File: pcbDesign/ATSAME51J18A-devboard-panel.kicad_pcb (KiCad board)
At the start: 2 copper layers, 100 x 100 mm, 294 parts, among them IC1 MP9361DJ-LF-P, J1 Micro_SD_Card, J10 CAN, J11 Conn_01x32_Male, J2 USB C, J3 QWIIC, J4 S2B-PH-K-S(LF)(SN), J7 Conn_01x32_Male, SW1 RST, U1 TCAN1051GVDRQ1, U2 ATSAME51J18A-A, U3 MIC5219-5.0YMM, U4 LM27762, U5 TPS60501DGS, U7 BQ24074RGT, U8 BQ27441DRZR-G1B, Y1 32.768

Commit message: Panelized with logo
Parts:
- removed the U2 at (93.4, 95.2)
- removed the U2 at (93.4, 63.7)
- removed the U4 at (103.5, 98.1)
- removed the U4 at (103.5, 66.6)
- added C21: 1u, Capacitor_SMD:C_0402_1005Metric, B.Cu at (107.2, 121.0)
- added C21: 1u, Capacitor_SMD:C_0402_1005Metric, B.Cu at (107.2, 89.6)
- added R12: 1.18k, Resistor_SMD:R_0402_1005Metric, B.Cu at (65.1, 130.5)
- added R12: 1.18k, Resistor_SMD:R_0402_1005Metric, B.Cu at (65.1, 99.1)
- U2 (x2): renamed from R12; value 1.18k -> ATSAME51J18A-A; footprint Resistor_SMD:R_0402_1005Metric -> Package_QFP:TQFP-64_10x10mm_P0.5mm; moved to F.Cu
- U4 (x2): renamed from C21; value 1u -> LM27762; footprint Capacitor_SMD:C_0402_1005Metric -> Package_SON:WSON-12-1EP_3x2mm_P0.5mm_EP1x2.65_ThermalVias
- moved U2 45.3 mm to (93.4, 95.2)
- moved U2 45.3 mm to (93.4, 63.7)
- moved U4 23.2 mm to (103.5, 98.1), turned to 0 degrees
- moved U4 23.2 mm to (103.5, 66.6), turned to 0 degrees
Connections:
- U2 pad 1: Board_3-GND -> Board_2-Net-(C4-Pad2)
- U2 pad 2: Board_3-Net-(R12-Pad2) -> Board_2-Net-(C3-Pad1)
- U2 pad 1: Board_2-GND -> Board_1-Net-(C4-Pad2)
- U2 pad 2: Board_2-Net-(R12-Pad2) -> Board_1-Net-(C3-Pad1)
- U4 pad 1: Board_3-Net-(C21-Pad1) -> Board_2-Net-(R6-Pad1)
- U4 pad 2: Board_3-Net-(C21-Pad2) -> Board_2-Net-(C15-Pad1)
- U4 pad 1: Board_2-Net-(C21-Pad1) -> Board_1-Net-(R6-Pad1)
- U4 pad 2: Board_2-Net-(C21-Pad2) -> Board_1-Net-(C15-Pad1)

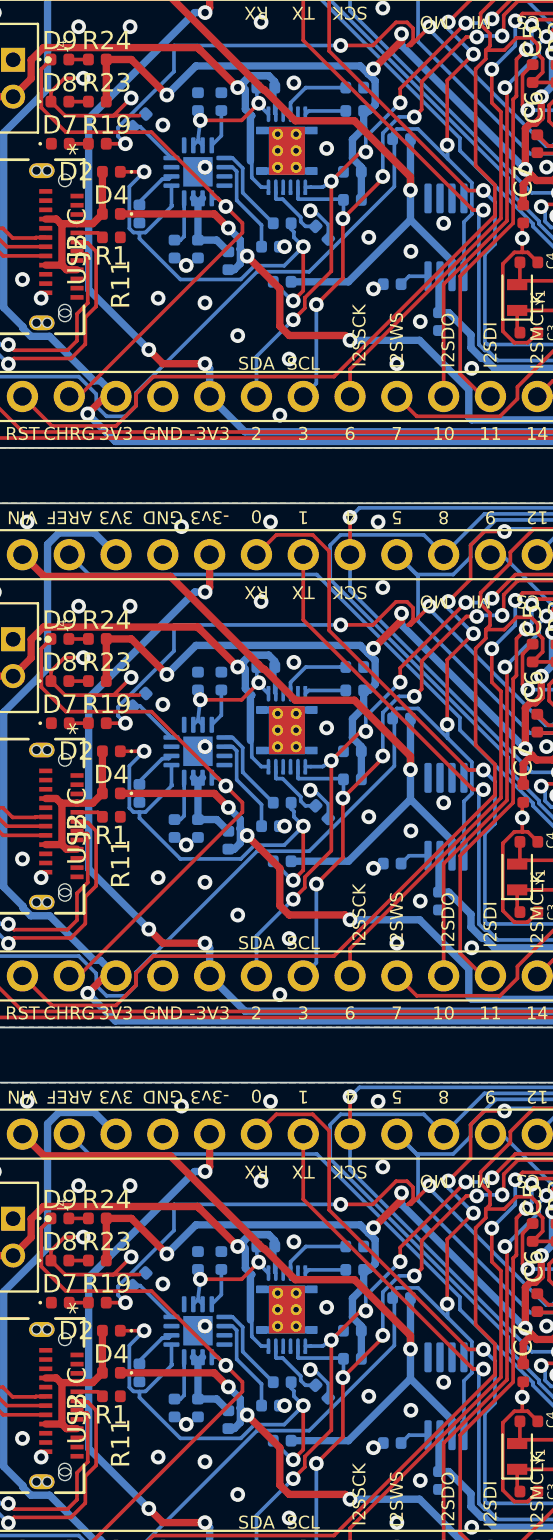
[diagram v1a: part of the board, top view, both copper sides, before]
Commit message: Panelized with logo
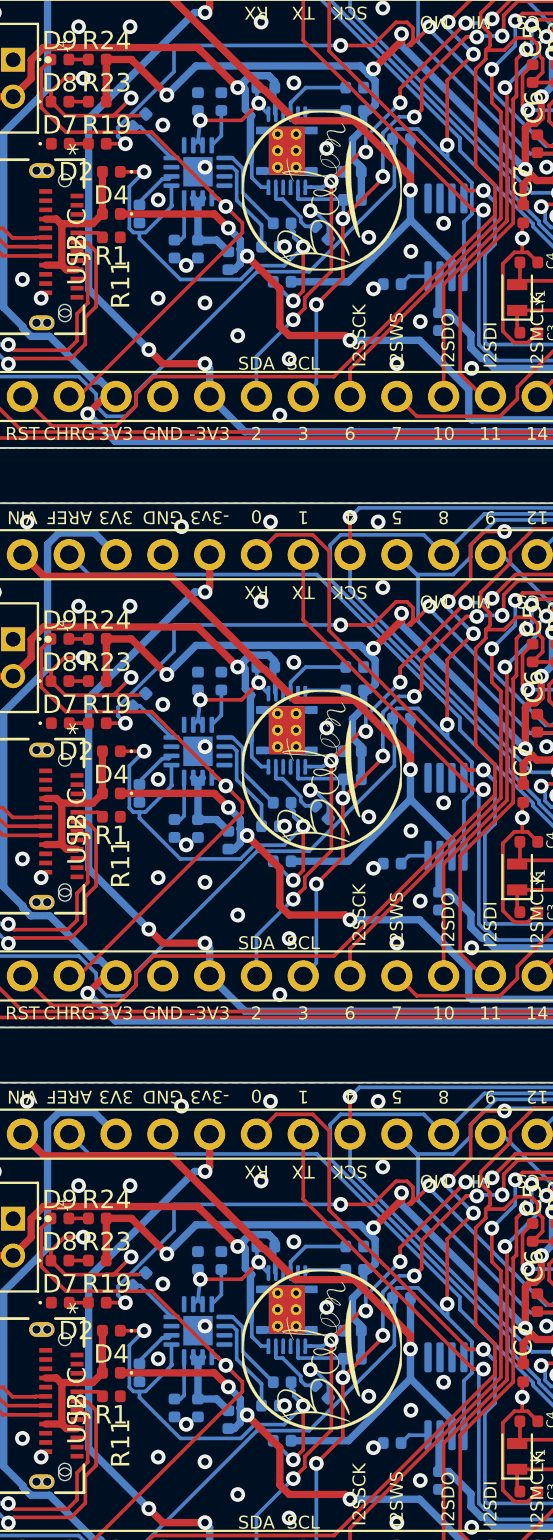
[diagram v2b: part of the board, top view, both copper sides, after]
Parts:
- removed the C18 at (112.7, 128.6)
- removed the C19 at (107.4, 123.8)
- removed the C20 at (102.3, 119.0)
- removed the C21 at (107.2, 121.0)
- removed the C22 at (66.4, 130.5)
- removed the C24 at (73.1, 129.7)
- removed the D4 at (61.7, 97.2)
- removed the R13 at (63.2, 123.6)
- removed the R14 at (74.8, 126.4)
- removed the R15 at (74.8, 127.9)
- removed the R16 at (70.1, 121.8)
- removed the R17 at (74.9, 121.8)
- removed the R18 at (74.9, 123.1)
- removed the R19 at (60.9, 124.8)
- added C1: 100n, Capacitor_SMD:C_0402_1005Metric, B.Cu at (123.2, 133.5)
- added C2: 100n, Capacitor_SMD:C_0402_1005Metric, B.Cu at (121.9, 123.3)
- added C3: 22u, Capacitor_SMD:C_0402_1005Metric, F.Cu at (84.3, 135.1)
- added C4: 22u, Capacitor_SMD:C_0402_1005Metric, F.Cu at (84.3, 131.3)
- added C5: 1u, Capacitor_SMD:C_0402_1005Metric, F.Cu at (84.5, 121.0)
- added C6: 1u, Capacitor_SMD:C_0402_1005Metric, F.Cu at (84.8, 124.8)
- added C7: 500n, Capacitor_SMD:C_0402_1005Metric, F.Cu at (84.0, 128.6)
- added G***: LOGO, Symbol:BatonLogo, F.Cu at (73.1, 127.4)
- added G***: LOGO, Symbol:BatonLogo, F.Cu at (73.1, 95.9)
- added G***: LOGO, Symbol:BatonLogo, F.Cu at (73.1, 64.5)
- added J1: Micro_SD_Card, Connector_Card:microSD_HC_Hirose_DM3D-SF, F.Cu at (125.4, 127.1)
- added R1: 5.1k, Resistor_SMD:R_0402_1005Metric, F.Cu at (61.7, 129.9)
- added R2: 5.1k, Resistor_SMD:R_0402_1005Metric, B.Cu at (54.1, 130.4)
- added R3: 10K, Resistor_SMD:R_0402_1005Metric, F.Cu at (85.8, 121.0)
- added R4: 10k, Resistor_SMD:R_0402_1005Metric, B.Cu at (77.4, 124.6)
- added R6: 10k, Resistor_SMD:R_0402_1005Metric, B.Cu at (101.6, 132.7)
- added R7: 87.5k, Resistor_SMD:R_0402_1005Metric, B.Cu at (106.8, 131.4)
- C10: renamed from C3; value 22u -> 2.2u; moved to B.Cu
- C11: renamed from C4; value 22u -> 4.7u; moved to B.Cu
- C12: renamed from C5; value 1u -> 2.2u; moved to B.Cu
- C13: renamed from C6; value 1u -> 4.7u; moved to B.Cu
- C14: renamed from C7; value 500n -> 0.47u; moved to B.Cu
- C15: renamed from C8; value 0.47u -> 2.2u
- C16: renamed from C9; value 0.47u -> 2.2u
- C17: renamed from C10; value 2.2u -> 1u
- C18: renamed from C11; value 4.7u -> 10u
- C19: renamed from C12; value 2.2u -> 4.7u
- C20: renamed from C13; value 4.7u -> 22u
- C21: renamed from C14; value 0.47u -> 1u
- C22: renamed from C15; value 2.2u -> 4.7u
- C23: renamed from C16; value 2.2u -> 4.7u
- C24: renamed from C17; value 1u -> 0.47u
- C8: renamed from C1; value 100n -> 0.47u
- C9: renamed from C2; value 100n -> 0.47u
- D4: renamed from C23; value 4.7u -> D_Schottky; footprint Capacitor_SMD:C_0402_1005Metric -> Diode_SMD:D_0402_1005Metric; moved to F.Cu
- R10: renamed from R2; value 5.1k -> 50k
- R11: renamed from R3; value 10K -> 46.4k; moved to B.Cu
- R12: renamed from R4; value 10k -> 1.18k
- R13: renamed from R6; value 10k -> 1.13k
- R14: renamed from R7; value 87.5k -> 5.1k
- R15: renamed from R8; value 87.5k -> 5.1k
- R16: renamed from R9; value 50k -> 0.01
- R17: renamed from R10; value 50k -> 10k
- R18: renamed from R11; value 46.4k -> 10k
- R19: renamed from R12; value 1.18k -> 10k; moved to F.Cu
- R8: renamed from J1; value Micro_SD_Card -> 87.5k; footprint Connector_Card:microSD_HC_Hirose_DM3D-SF -> Resistor_SMD:R_0402_1005Metric; moved to B.Cu
- R9: renamed from R1; value 5.1k -> 50k; moved to B.Cu
- moved R10 52.7 mm to (106.6, 127.6)
- moved C8 46.2 mm to (76.9, 132.5), turned to 180 degrees
- moved R9 45.2 mm to (106.8, 133.3), turned to 270 degrees
- moved C22 41.5 mm to (66.4, 130.5), turned to 270 degrees
- moved R13 39.4 mm to (63.2, 123.6), turned to 45 degrees
- moved R16 38.5 mm to (70.1, 121.8), turned to 0 degrees
- moved C23 37.8 mm to (66.4, 122.5), turned to 90 degrees
- moved R14 32.4 mm to (74.8, 126.4), turned to 180 degrees
- moved R17 32.3 mm to (74.9, 121.8), turned to 0 degrees
- moved C23 31.4 mm to (66.4, 91.1)
- moved C10 31.4 mm to (113.0, 122.3), turned to 270 degrees
- moved C15 31.0 mm to (107.9, 131.4), turned to 90 degrees
- moved C19 29.9 mm to (107.4, 123.8)
- moved R15 29.4 mm to (74.8, 127.9), turned to 0 degrees
- moved C24 27.7 mm to (73.1, 129.7), turned to 315 degrees
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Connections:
- C10 pad 1: Board_3-Net-(C3-Pad1) -> Board_3-VBUS_NREG
- C11 pad 2: Board_3-Net-(C4-Pad2) -> Board_3-VBUS_NREG
- C12 pad 1: Board_3-GND -> Board_3-VBUS_VIN_5V_REG
- C12 pad 2: Board_3-RST -> Board_3-GND
- C13 pad 1: Board_3-GND -> Board_3-Net-(C13-Pad1)
- C13 pad 2: Board_3-Net-(C6-Pad2) -> Board_3-GND
- C14 pad 1: Board_3-GND -> Board_3-Net-(C14-Pad1)
- C14 pad 2: Board_3-VBUS_3V3_CH0_REG -> Board_3-Net-(C14-Pad2)
- C15 pad 1: Board_3-Net-(C8-Pad1) -> Board_3-Net-(C15-Pad1)
- C15 pad 2: Board_3-GND -> Board_3-VBUS_3V3_CH1_REG
- C16 pad 1: Board_3-Net-(C9-Pad1) -> Board_3-VBUS_-3V3_CH2_REG
- C16 pad 2: Board_3-Net-(C9-Pad2) -> Board_3-Net-(C16-Pad2)
- C17 pad 1: Board_3-VBUS_NREG -> Board_3-Net-(C17-Pad1)
- C17 pad 2: Board_3-GND -> Board_3-Net-(C17-Pad2)
- C18 pad 2: Board_3-VBUS_NREG -> Board_3-+5V
- C19 pad 1: Board_3-VBUS_VIN_5V_REG -> Board_3-VBUS_NREG
- C20 pad 1: Board_3-Net-(C13-Pad1) -> Board_3-GND
- C20 pad 2: Board_3-GND -> Board_3-VBUS_3V3_CH0_REG
- C21 pad 1: Board_3-Net-(C14-Pad1) -> Board_3-Net-(C21-Pad1)
- C21 pad 2: Board_3-Net-(C14-Pad2) -> Board_3-Net-(C21-Pad2)
- C22 pad 1: Board_3-Net-(C15-Pad1) -> Board_3-VBUS_BAT_NREG
- C22 pad 2: Board_3-VBUS_3V3_CH1_REG -> Board_3-GND
- C23 pad 1: Board_3-VBUS_-3V3_CH2_REG -> Board_3-Net-(C23-Pad1)
- C23 pad 2: Board_3-Net-(C16-Pad2) -> Board_3-GND
- C23 pad 1: Board_3-Net-(C23-Pad1) -> Board_2-Net-(C23-Pad1)
- C23 pad 2: Board_3-GND -> Board_2-GND
- C24 pad 1: Board_3-Net-(C17-Pad1) -> Board_3-Net-(C24-Pad1)
- C24 pad 2: Board_3-Net-(C17-Pad2) -> Board_3-GND
- C8 pad 1: Board_3-GND -> Board_3-Net-(C8-Pad1)
- C8 pad 2: Board_3-VBUS_3V3_CH0_REG -> Board_3-GND
- C9 pad 1: Board_3-GND -> Board_3-Net-(C9-Pad1)
- C9 pad 2: Board_3-+5V -> Board_3-Net-(C9-Pad2)
- D4 pad 1: Board_2-Net-(C23-Pad1) -> Board_2-VBUS_NREG
- D4 pad 2: Board_2-GND -> Board_2-VBUS_USB_NREG
- R10 pad 1: Board_3-Net-(J2-PadB5) -> Board_3-GND
- R10 pad 2: Board_3-GND -> Board_3-Net-(C16-Pad2)
- R11 pad 1: Board_3-RST -> Board_3-GND
- R11 pad 2: Board_3-VBUS_3V3_CH0_REG -> Board_3-Net-(R11-Pad2)
- R12 pad 1: Board_3-VBUS_VIN_NREG -> Board_3-GND
- R12 pad 2: Board_3-EN -> Board_3-Net-(R12-Pad2)
- R13 pad 1: Board_3-Net-(R6-Pad1) -> Board_3-Net-(R13-Pad1)
- R13 pad 2: Board_3-VBUS_NREG -> Board_3-GND
- R14 pad 1: Board_3-VBUS_3V3_CH1_REG -> Board_3-VBUS_3V3_CH0_REG
- R14 pad 2: Board_3-Net-(C15-Pad1) -> Board_3-2[SDA]
- R15 pad 1: Board_3-Net-(C16-Pad2) -> Board_3-3[SCL]
- R15 pad 2: Board_3-VBUS_-3V3_CH2_REG -> Board_3-VBUS_3V3_CH0_REG
- R16 pad 1: Board_3-Net-(C15-Pad1) -> Board_3-Net-(C23-Pad1)
- R16 pad 2: Board_3-GND -> Board_3-VBUS_BAT
- R17 pad 1: Board_3-GND -> Board_3-Net-(R17-Pad1)
- R17 pad 2: Board_3-Net-(C16-Pad2) -> Board_3-GND
- R18 pad 1: Board_3-GND -> Board_3-Net-(R18-Pad1)
- R18 pad 2: Board_3-Net-(R11-Pad2) -> Board_3-VBUS_3V3_CH0_REG
- R19 pad 1: Board_3-GND -> Board_3-13
- R19 pad 2: Board_3-Net-(R12-Pad2) -> Board_3-Net-(D7-Pad2)
- R8 pad 1: (no net) -> Board_3-Net-(C16-Pad2)
- R8 pad 2: Board_3-SDDAT3 -> Board_3-VBUS_-3V3_CH2_REG
- R9 pad 1: Board_3-GND -> Board_3-Net-(C15-Pad1)
- R9 pad 2: Board_3-Net-(J2-PadA5) -> Board_3-GND
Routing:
- net Board_3-GND: vias 80 -> 81
- net Board_2-GND: vias 80 -> 81
- net Board_1-GND: vias 80 -> 81

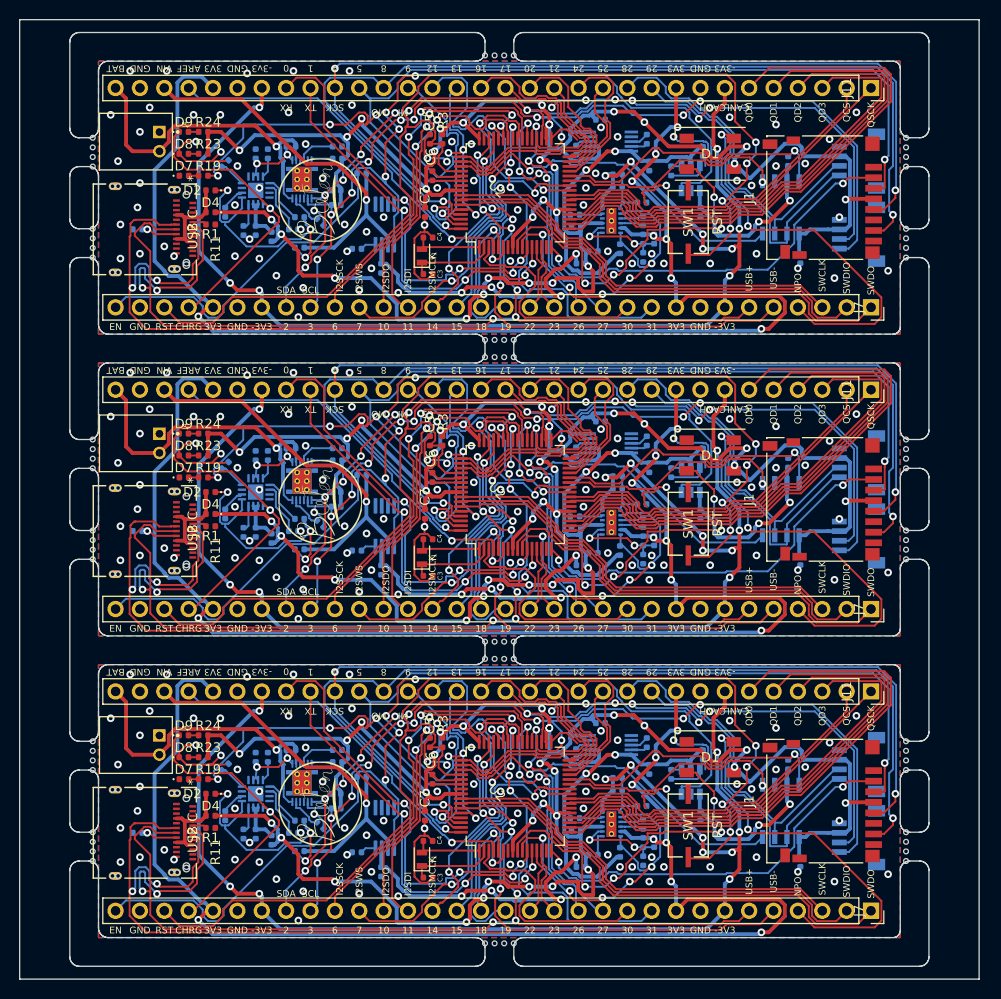
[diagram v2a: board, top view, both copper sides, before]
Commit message: Fixed some DRC errors
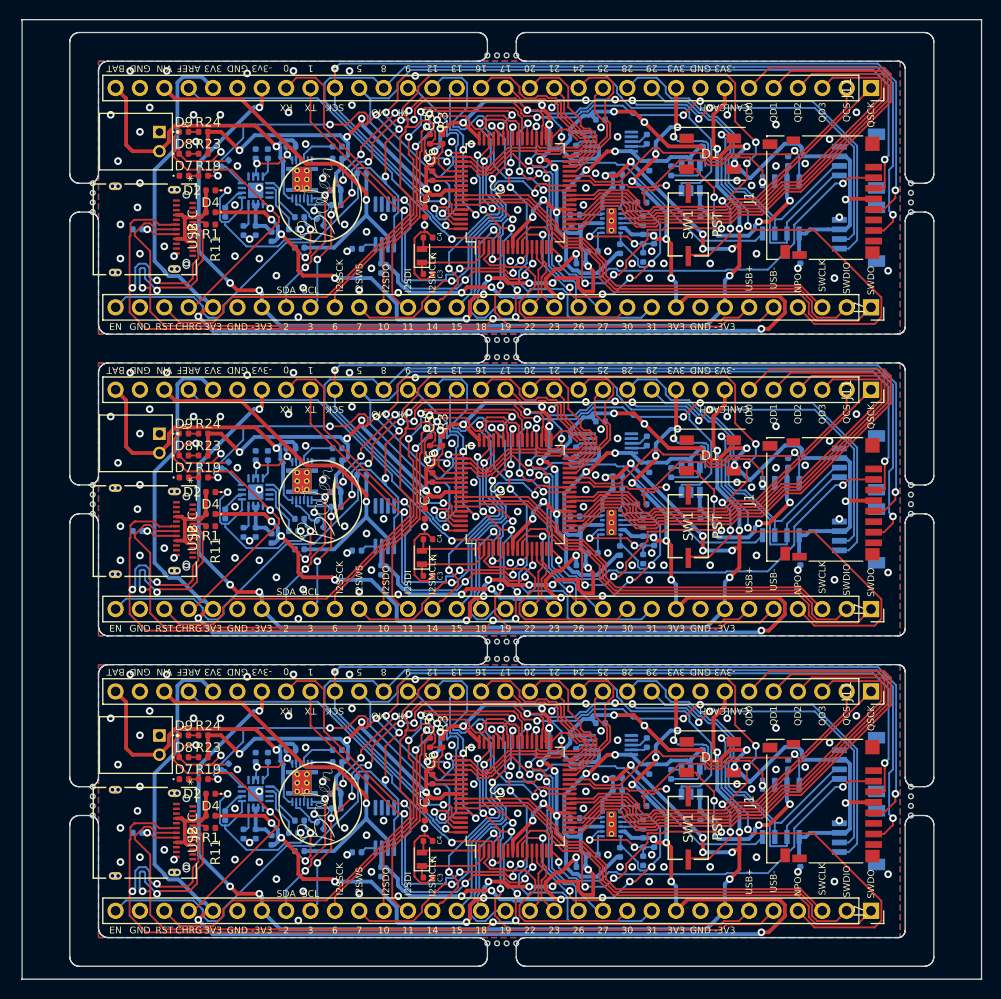
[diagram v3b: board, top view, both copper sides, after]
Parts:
- removed the REF** at (134.2, 130.4)
- removed the REF** at (49.4, 132.4)
- removed the REF** at (49.4, 131.4)
- removed the REF** at (49.4, 130.4)
- removed the REF** at (49.4, 123.9)
- removed the REF** at (49.4, 122.9)
- removed the REF** at (49.4, 121.9)
- removed the REF** at (49.4, 120.9)
- removed the REF** at (134.2, 98.9)
- removed the REF** at (134.2, 99.9)
- removed the REF** at (134.2, 100.9)
- removed the REF** at (134.2, 131.4)
- removed the REF** at (134.2, 101.9)
- removed the REF** at (134.2, 89.4)
- removed the REF** at (134.2, 90.4)
- removed the REF** at (134.2, 91.4)
- removed the REF** at (134.2, 92.4)
- removed the REF** at (49.4, 101.9)
- removed the REF** at (49.4, 100.9)
- removed the REF** at (49.4, 99.9)
- removed the REF** at (49.4, 98.9)
- removed the REF** at (49.4, 92.4)
- removed the REF** at (134.2, 132.4)
- removed the REF** at (49.4, 91.4)
- removed the REF** at (49.4, 90.4)
- removed the REF** at (49.4, 89.4)
- removed the REF** at (134.2, 67.5)
- removed the REF** at (134.2, 68.5)
- removed the REF** at (134.2, 69.5)
- removed the REF** at (134.2, 70.5)
- removed the REF** at (134.2, 58.0)
- removed the REF** at (134.2, 59.0)
- removed the REF** at (134.2, 60.0)
- removed the REF** at (134.2, 133.4)
- removed the REF** at (134.2, 61.0)
- removed the REF** at (49.4, 70.5)
- removed the REF** at (49.4, 69.5)
- removed the REF** at (49.4, 68.5)
- removed the REF** at (49.4, 67.5)
- removed the REF** at (49.4, 61.0)
- removed the REF** at (49.4, 60.0)
- removed the REF** at (49.4, 59.0)
- removed the REF** at (49.4, 58.0)
- removed the REF** at (93.3, 141.9)
- removed the REF** at (134.2, 120.9)
- removed the REF** at (92.3, 141.9)
- removed the REF** at (91.3, 141.9)
- removed the REF** at (90.3, 141.9)
- removed the REF** at (90.3, 112.3)
- removed the REF** at (91.3, 112.3)
- removed the REF** at (92.3, 112.3)
- removed the REF** at (93.3, 112.3)
- removed the REF** at (93.3, 110.5)
- removed the REF** at (92.3, 110.5)
- removed the REF** at (91.3, 110.5)
- removed the REF** at (134.2, 121.9)
- removed the REF** at (90.3, 110.5)
- removed the REF** at (90.3, 80.8)
- removed the REF** at (91.3, 80.8)
- removed the REF** at (92.3, 80.8)
- removed the REF** at (93.3, 80.8)
- removed the REF** at (93.3, 79.0)
- removed the REF** at (92.3, 79.0)
- removed the REF** at (91.3, 79.0)
- removed the REF** at (90.3, 79.0)
- removed the REF** at (90.3, 49.4)
- removed the REF** at (134.2, 122.9)
- removed the REF** at (91.3, 49.4)
- removed the REF** at (92.3, 49.4)
- removed the REF** at (93.3, 49.4)
- removed the REF** at (134.2, 123.9)
- removed the REF** at (49.4, 133.4)
- removed the SW1 at (111.5, 129.7)
- removed the SW1 at (111.5, 98.2)
- removed the SW1 at (111.5, 66.8)
- added REF**: NPTH, NPTH, F.Cu at (134.7, 125.6)
- added REF**: NPTH, NPTH, F.Cu at (134.7, 95.2)
- added REF**: NPTH, NPTH, F.Cu at (134.7, 96.2)
- added REF**: NPTH, NPTH, F.Cu at (134.7, 97.2)
- added REF**: NPTH, NPTH, F.Cu at (49.4, 97.2)
- added REF**: NPTH, NPTH, F.Cu at (49.4, 96.2)
- added REF**: NPTH, NPTH, F.Cu at (49.4, 95.2)
- added REF**: NPTH, NPTH, F.Cu at (49.4, 94.2)
- added REF**: NPTH, NPTH, F.Cu at (134.7, 62.7)
- added REF**: NPTH, NPTH, F.Cu at (134.7, 63.7)
- added REF**: NPTH, NPTH, F.Cu at (134.7, 64.7)
- added REF**: NPTH, NPTH, F.Cu at (134.7, 126.6)
- added REF**: NPTH, NPTH, F.Cu at (134.7, 65.7)
- added REF**: NPTH, NPTH, F.Cu at (49.4, 65.7)
- added REF**: NPTH, NPTH, F.Cu at (49.4, 64.7)
- added REF**: NPTH, NPTH, F.Cu at (49.4, 63.7)
- added REF**: NPTH, NPTH, F.Cu at (49.4, 62.7)
- added REF**: NPTH, NPTH, F.Cu at (93.5, 141.9)
- added REF**: NPTH, NPTH, F.Cu at (92.5, 141.9)
- added REF**: NPTH, NPTH, F.Cu at (91.5, 141.9)
- added REF**: NPTH, NPTH, F.Cu at (90.5, 141.9)
- added REF**: NPTH, NPTH, F.Cu at (90.5, 112.3)
- added REF**: NPTH, NPTH, F.Cu at (134.7, 127.6)
- added REF**: NPTH, NPTH, F.Cu at (91.5, 112.3)
- added REF**: NPTH, NPTH, F.Cu at (92.5, 112.3)
- added REF**: NPTH, NPTH, F.Cu at (93.5, 112.3)
- added REF**: NPTH, NPTH, F.Cu at (93.5, 110.5)
- added REF**: NPTH, NPTH, F.Cu at (92.5, 110.5)
- added REF**: NPTH, NPTH, F.Cu at (91.5, 110.5)
- added REF**: NPTH, NPTH, F.Cu at (90.5, 110.5)
- added REF**: NPTH, NPTH, F.Cu at (90.5, 80.8)
- added REF**: NPTH, NPTH, F.Cu at (91.5, 80.8)
- added REF**: NPTH, NPTH, F.Cu at (92.5, 80.8)
- added REF**: NPTH, NPTH, F.Cu at (134.7, 128.6)
- added REF**: NPTH, NPTH, F.Cu at (93.5, 80.8)
- added REF**: NPTH, NPTH, F.Cu at (93.5, 79.0)
- added REF**: NPTH, NPTH, F.Cu at (92.5, 79.0)
- added REF**: NPTH, NPTH, F.Cu at (91.5, 79.0)
- added REF**: NPTH, NPTH, F.Cu at (90.5, 79.0)
- added REF**: NPTH, NPTH, F.Cu at (90.5, 49.4)
- added REF**: NPTH, NPTH, F.Cu at (91.5, 49.4)
- added REF**: NPTH, NPTH, F.Cu at (92.5, 49.4)
- added REF**: NPTH, NPTH, F.Cu at (93.5, 49.4)
- added REF**: NPTH, NPTH, F.Cu at (49.4, 128.6)
- added REF**: NPTH, NPTH, F.Cu at (49.4, 127.6)
- added REF**: NPTH, NPTH, F.Cu at (49.4, 126.6)
- added REF**: NPTH, NPTH, F.Cu at (49.4, 125.6)
- added REF**: NPTH, NPTH, F.Cu at (134.7, 94.2)
- added SW1: RST, PTS636:PTS636 SM25F SMTR LFS, F.Cu at (111.5, 129.9)
- added SW1: RST, PTS636:PTS636 SM25F SMTR LFS, F.Cu at (111.5, 98.5)
- added SW1: RST, PTS636:PTS636 SM25F SMTR LFS, F.Cu at (111.5, 67.0)
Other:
- outline, holes or cut-outs redrawn
